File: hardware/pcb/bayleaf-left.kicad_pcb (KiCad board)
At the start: 2 copper layers, 135.5 x 89.5 mm, 64 parts, among them SW1 PG1316S, SW10 PG1316S, SW11 PG1316S, SW12 PG1316S, SW13 PG1316S, SW14 PG1316S, SW15 PG1316S, SW16 PG1316S, SW17 PG1316S, SW18 PG1316S, SW19 PG1316S, SW2 PG1316S, SW20 PG1316S, SW21 PG1316S, SW22 PG1316S, SW23 PG1316S, SW24 PG1316S, SW25 PG1316S, SW26 PG1316S, SW27 PG1316S, SW28 PG1316S, SW29 PG1316S, SW3 PG1316S, SW30 PG1316S, SW31 TS-1187A-B-A-B, SW32 MSK12C02, SW4 PG1316S, SW5 PG1316S, SW6 PG1316S, SW7 PG1316S, SW8 PG1316S, SW9 PG1316S, U1 nice!nano v2

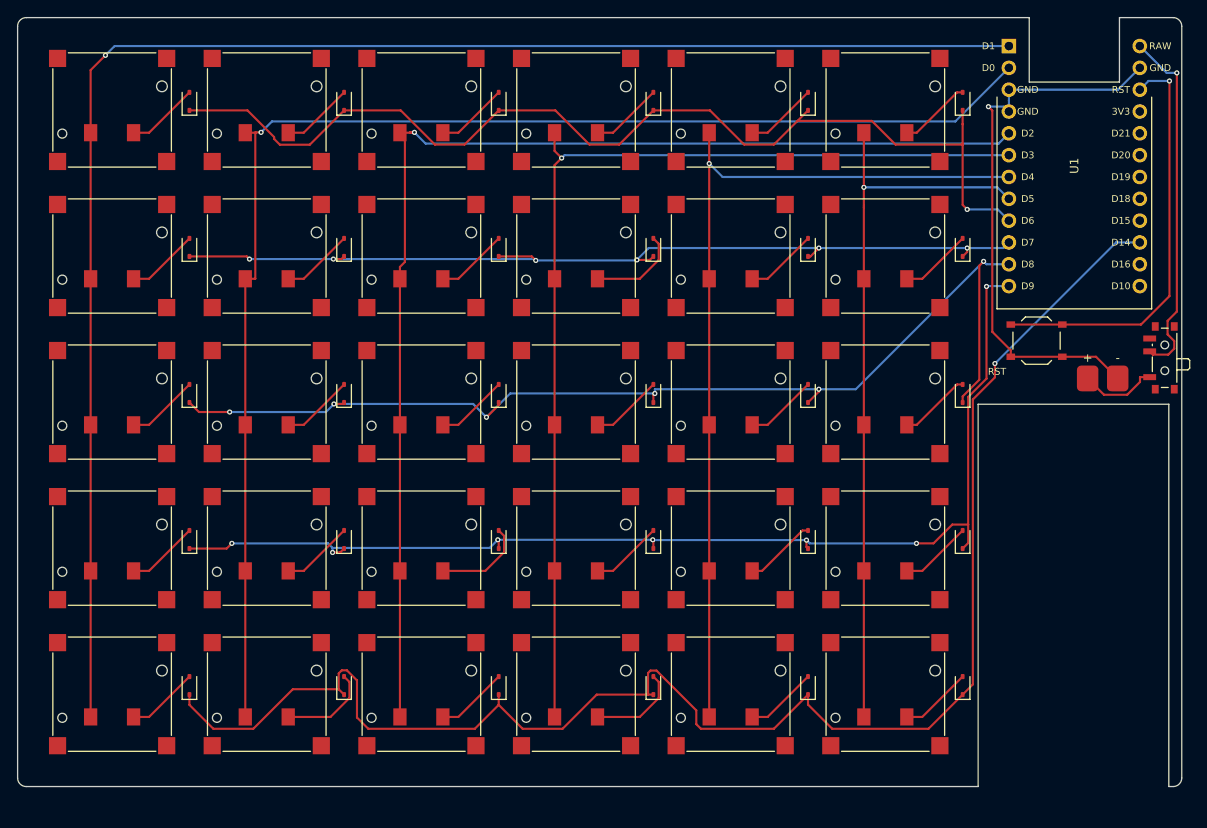
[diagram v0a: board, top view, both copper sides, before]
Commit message: Case: rebuild after the original's MK5 drawing (shell + lid over controller)
- hardware/case: top shell with 103 x 86 key window, 2 mm divider, 27 mm
  controller bay closed by a 0.8 mm roof, 6.2 -> 3.8 mm front curve, drafted
  walls, 7 tapped M2 bosses; separate 0.8 mm bottom plate screwed into them
- PCB: 17 mm pitch to fit the window, SOD-523 diodes, nice!nano rotated so
  USB-C exits the front, 402040 cell under the roof, 2.2 mm holes + copper
  keep-outs at the bosses, per-half matrix pin map; both halves route clean
- firmware: per-half kscan pins in the left/right overlays
- docs: case-drawing notes, BOM/ordering/assembly/schematic, new renders

Co-Authored-By: Claude Opus 5.5 <noreply@anthropic.com>
Claude-Session: https://claude.ai/code/session_01C1HRLCKaYQawWFomwAvAgT
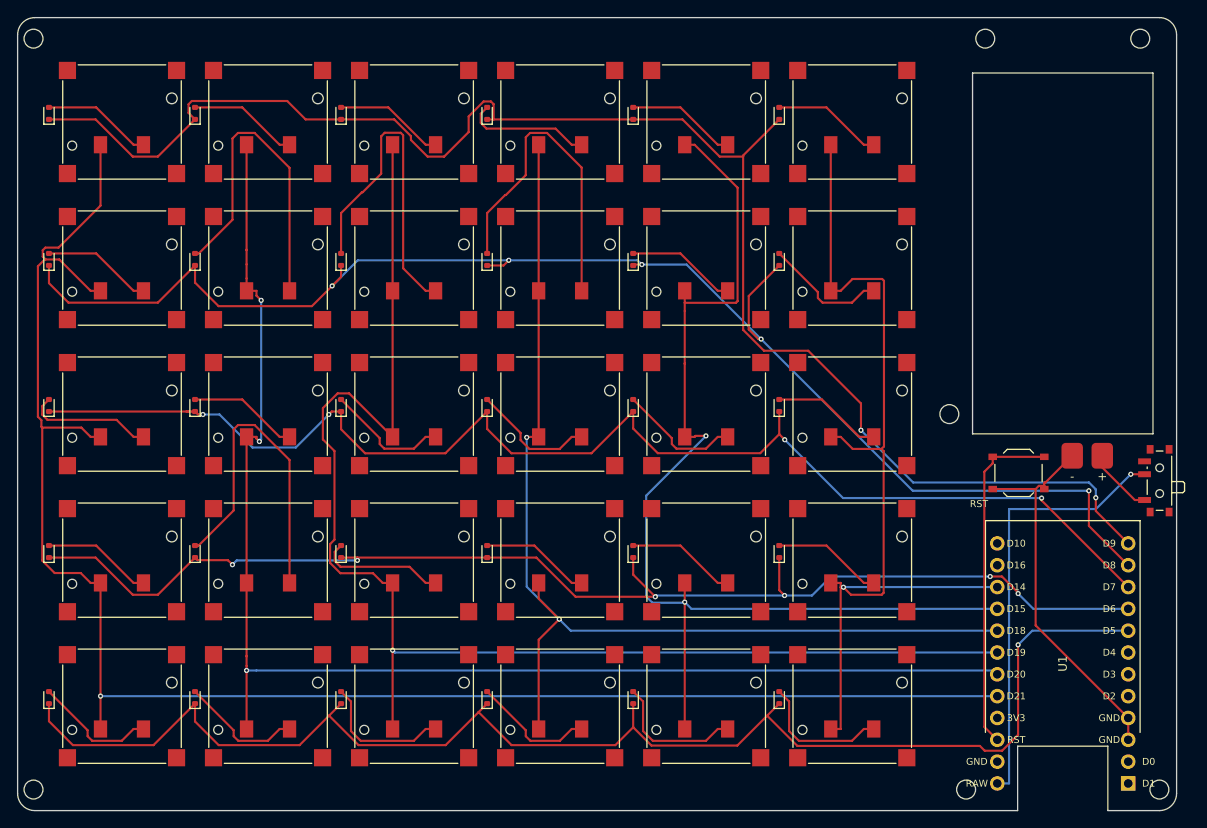
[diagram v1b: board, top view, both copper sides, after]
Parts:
- added H1: boss 6, MountingHole:MountingHole_2.2mm_M2, F.Cu at (1.85, 2.45)
- added H2: boss 6, MountingHole:MountingHole_2.2mm_M2, F.Cu at (1.85, 89.8)
- added H3: boss 6, MountingHole:MountingHole_2.2mm_M2, F.Cu at (112.6, 2.45)
- added H4: boss 6, MountingHole:MountingHole_2.2mm_M2, F.Cu at (130.7, 2.45)
- added H5: boss 6, MountingHole:MountingHole_2.2mm_M2, F.Cu at (108.5, 46.1)
- added H6: boss 4, MountingHole:MountingHole_2.2mm_M2, F.Cu at (110.4, 89.8)
- added H7: boss 4, MountingHole:MountingHole_2.2mm_M2, F.Cu at (132.9, 89.8)
- D1, D10, D11, D12, D13, D14, D15, D16, D17, D18, D19, D2, D20, D21, D22, D23, D24, D25, D26, D27, D28, D29, D3, D30, D4, D5, D6, D7, D8, D9: value 1N4148WS -> 1N4148WT; footprint Diode_SMD:D_SOD-323 -> Diode_SMD:D_SOD-523
- moved U1 58.0 mm to (121.7, 75.2), turned to 180 degrees
- moved D12 21.4 mm to (88.7, 28.1)
- moved D18 21.4 mm to (88.7, 45.1)
- moved D24 21.4 mm to (88.7, 62.1)
- moved D30 21.4 mm to (88.7, 79.2)
- moved D6 21.4 mm to (88.7, 11.2)
- moved D11 20.4 mm to (71.7, 28.1)
- moved D17 20.4 mm to (71.7, 45.1)
- moved D23 20.4 mm to (71.7, 62.1)
- moved D29 20.4 mm to (71.7, 79.2)
- moved D5 20.4 mm to (71.7, 11.2)
- moved D10 19.4 mm to (54.6, 28.1)
- moved D16 19.4 mm to (54.6, 45.1)
- moved D22 19.4 mm to (54.6, 62.1)
- moved D28 19.4 mm to (54.6, 79.2)
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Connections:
- U1 pad 1: COL0 -> (no net)
- U1 pad 10: ROW1 -> ROW2
- U1 pad 11: ROW2 -> ROW1
- U1 pad 12: ROW3 -> ROW0
- U1 pad 14: GND -> (no net)
- U1 pad 17: (no net) -> COL0
- U1 pad 18: (no net) -> COL1
- U1 pad 19: (no net) -> COL2
- U1 pad 2: COL1 -> (no net)
- U1 pad 20: (no net) -> COL3
- U1 pad 21: (no net) -> COL4
- U1 pad 22: ROW4 -> COL5
- U1 pad 5: COL2 -> (no net)
- U1 pad 6: COL3 -> (no net)
- U1 pad 7: COL4 -> (no net)
- U1 pad 8: COL5 -> ROW4
- U1 pad 9: ROW0 -> ROW3
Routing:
- net ROW1: track 107.3 -> 170.3 mm, vias 6 -> 5
- net ROW0: track 122.8 -> 183.1 mm, vias 1 -> 2
- net N_SW9: track 8.45 -> 38.8 mm
- net N_SW8: track 8.45 -> 38.4 mm
- net N_SW20: track 8.45 -> 38.3 mm
- net N_SW10: track 10.8 -> 38.2 mm
- net ROW2: track 129.0 -> 153.8 mm, vias 6 -> 4
- net COL5: track 85.4 -> 109.6 mm
- net COL4: track 103.5 -> 127.3 mm, vias 1 -> 2
- net GND: track 65.1 -> 45.1 mm, vias 1 -> 0
- net COL2: track 140.8 -> 159.4 mm
- net ROW4: track 183.0 -> 165.0 mm
- net ROW3: track 132.2 -> 146.8 mm, vias 7 -> 6
- net COL0: track 183.3 -> 197.2 mm
- net RAW: track 41.8 -> 50.8 mm
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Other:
- board size 135.5 x 89.5 mm -> 134.9 x 92.3 mm
- board text added: "LiPo 4.0x20x40"
- board text removed: "LiPo 3.0x20x40"

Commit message: Case: match the build photos - 5 mm tall, separate controller lid
- shell: 3.8 mm frame around the key window curving up to 4.1 mm at the
  controller end; controller bay now open on top; all posts M2 x 2
- new lid part: 0.8 mm plate over the bay, flush with the outer edges, taped
  on; its top is the 5.0 mm tallest point (contrast anodised like the original)
- 302040 cell (bay under the lid is 3.4 mm), 14 x M2x3 screws
- renders: silver shell, blue lid, blank caps; desk/front views like the photos
- docs/BOM/README updated; PCB unchanged

Co-Authored-By: Claude Opus 5.5 <noreply@anthropic.com>
Claude-Session: https://claude.ai/code/session_01C1HRLCKaYQawWFomwAvAgT
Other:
- board text added: "LiPo 3.0x20x40"
- board text removed: "LiPo 4.0x20x40"
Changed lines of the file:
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@@
     (effects (font (size 0.8 0.8) (thickness 0.12)))
   )
-  (gr_text "LiPo 4.0x20x40" (at 121.65 27) (layer "Cmts.User")
+  (gr_text "LiPo 3.0x20x40" (at 121.65 27) (layer "Cmts.User")
     (effects (font (size 0.9 0.9) (thickness 0.135)))
   )

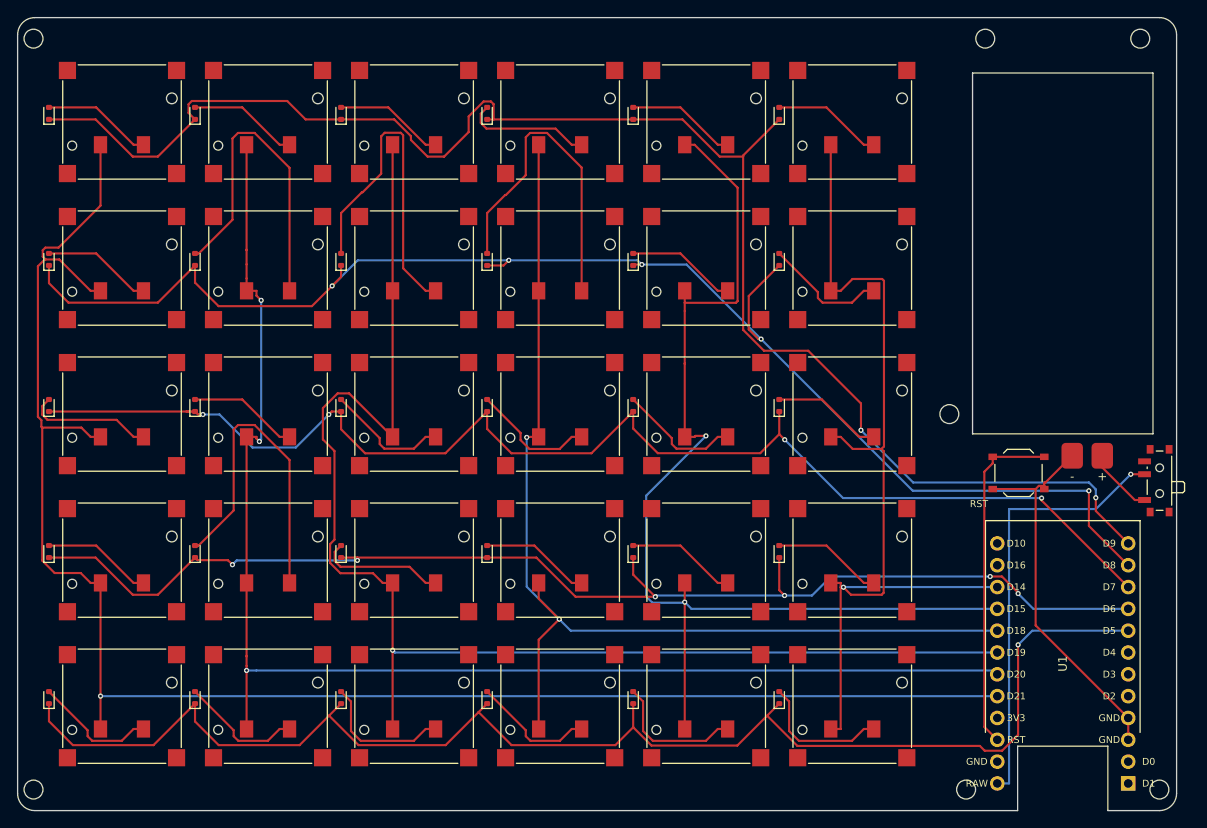
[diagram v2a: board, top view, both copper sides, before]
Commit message: Case: one-piece shell from the sketchpad shape (3.2 mm rim, 5.0 mm plateau, S-bends)
- case.py: top surface = blurred square plateau (x >= 96.5, y <= 76) over a 3.2 mm rim;
  controller roofed by the shell (no lid), R2 key-window corners, USB-C in the back wall,
  reset pin-hole, per-post thread depths (2 mm / 1.1 mm)
- PCB: nice!nano USB-C facing the back, KMR2 reset and slide switch beside it, 302030 cell
  window in front of it; rerouted, fab outputs regenerated
- firmware: per-half matrix pins to match the new layout
- docs: sketchpad shape saved, renders, BOM/ordering/assembly/case/schematic updated

Co-Authored-By: Claude Opus 5.5 <noreply@anthropic.com>
Claude-Session: https://claude.ai/code/session_01C1HRLCKaYQawWFomwAvAgT
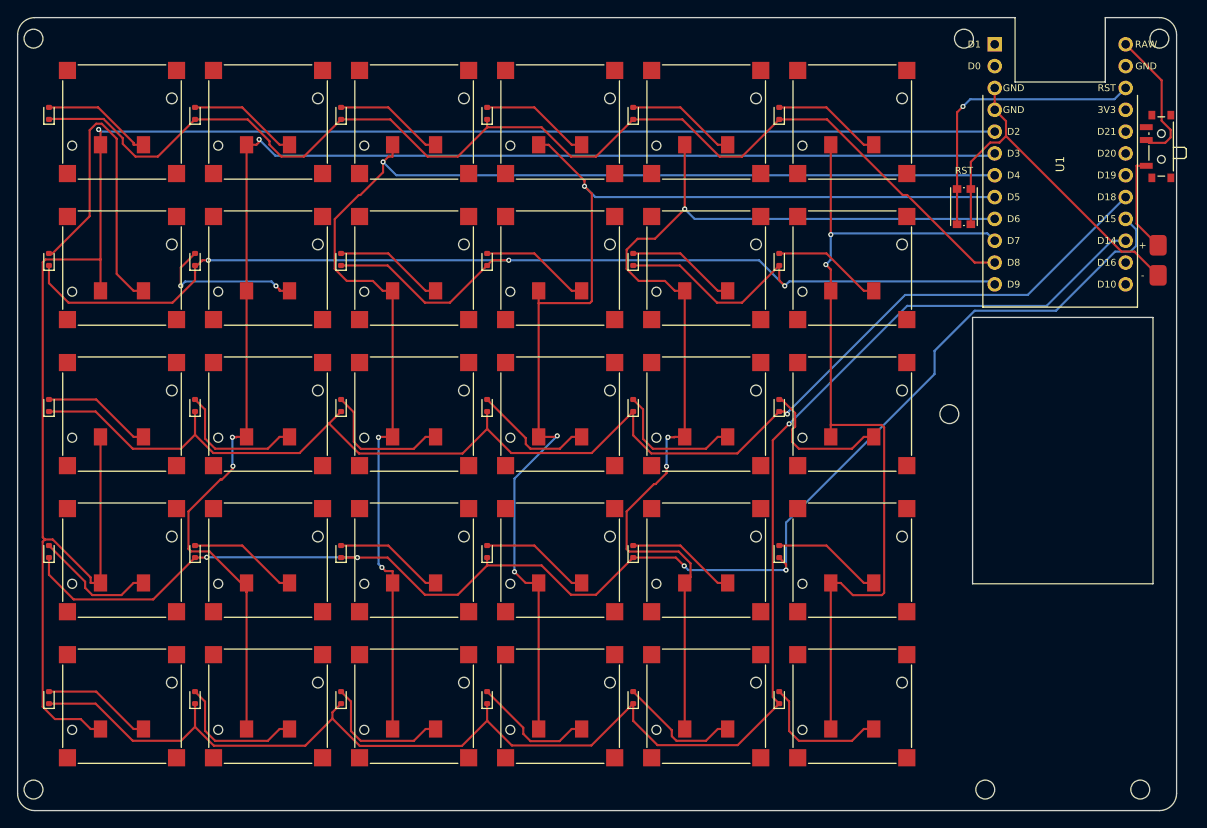
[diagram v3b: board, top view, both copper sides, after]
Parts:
- BT1: footprint bayleaf:Battery_Pads -> bayleaf:Battery_Pads_Small
- H3, H4: value boss 6 -> boss 4
- H6, H7: value boss 4 -> boss 6
- SW31: value TS-1187A-B-A-B -> KMR211NGLFS; footprint Button_Switch_SMD:SW_Push_1P1T_XKB_TS-1187A -> Button_Switch_SMD:SW_Push_1P1T_NO_CK_KMR2
- moved U1 58.2 mm to (121.3, 17.0), turned to 0 degrees
- moved SW32 38.9 mm to (132.8, 15.0)
- moved SW31 31.6 mm to (110.2, 22.0), turned to 90 degrees
- moved BT1 24.2 mm to (132.8, 28.2), turned to 0 degrees
- moved H3 2.48 mm to (110.2, 2.45)
- moved H4 2.23 mm to (132.9, 2.45)
- moved H7 2.23 mm to (130.7, 89.8)
- moved H6 2.23 mm to (112.6, 89.8)
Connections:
- U1 pad 10: ROW2 -> COL5
- U1 pad 11: ROW1 -> ROW0
- U1 pad 12: ROW0 -> ROW1
- U1 pad 17: COL0 -> (no net)
- U1 pad 18: COL1 -> (no net)
- U1 pad 19: COL2 -> (no net)
- U1 pad 20: COL3 -> ROW2
- U1 pad 21: COL4 -> ROW3
- U1 pad 22: COL5 -> ROW4
- U1 pad 5: (no net) -> COL0
- U1 pad 6: (no net) -> COL1
- U1 pad 7: (no net) -> COL2
- U1 pad 8: ROW4 -> COL3
- U1 pad 9: ROW3 -> COL4
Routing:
- net ROW0: track 183.1 -> 135.7 mm, vias 2 -> 0
- net RAW: track 50.8 -> 16.2 mm, vias 1 -> 0
- net N_SW7: track 12.8 -> 40.4 mm
- net N_SW9: track 38.8 -> 12.8 mm
- net N_SW20: track 38.3 -> 12.8 mm
- net N_SW10: track 38.2 -> 12.8 mm
- net ROW4: track 165.0 -> 189.1 mm
- net ROW3: track 146.8 -> 167.5 mm, vias 6 -> 4
- net N_SW8: track 38.4 -> 17.9 mm, vias 0 -> 2
- net COL0: track 197.2 -> 215.8 mm
- net COL2: track 159.4 -> 151.0 mm, vias 1 -> 3
- net RST: track 40.0 -> 33.8 mm, vias 0 -> 1
- net COL5: track 109.6 -> 103.5 mm, vias 1 -> 2
- net COL1: track 159.8 -> 165.4 mm
- net ROW1: track 170.3 -> 165.0 mm, vias 5 -> 3
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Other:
- outline, holes or cut-outs redrawn
- board text added: "LiPo 3.0x20x30"
- board text removed: "LiPo 3.0x20x40"

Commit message: Drop the power switch, stadium USB-C opening, straight-wall + chamfer case variant
- PCB: no slide switch; the cell feeds the nice!nano RAW pin directly (ZMK deep sleep);
  rerouted, 0 unconnected, courtyard warning gone
- case: obround USB-C opening concentric with the receptacle (continues into the plate
  edge), no switch slot; new bayleaf-shell-*-chamfer variant with vertical walls and a
  1 mm 45 deg chamfer on the top edge that follows the blended surface
- renders: obround receptacle, compare.jpg (drafted vs chamfer); docs and BOM updated

Co-Authored-By: Claude Opus 5.5 <noreply@anthropic.com>
Claude-Session: https://claude.ai/code/session_01C1HRLCKaYQawWFomwAvAgT
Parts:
- removed SW32: MSK12C02, Button_Switch_SMD:SW_SPDT_PCM12
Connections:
- BT1 pad 1: BAT+ -> RAW
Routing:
- net COL1: track 165.4 -> 194.2 mm, vias 3 -> 1
- net ROW2: track 158.9 -> 186.4 mm, vias 1 -> 3
- net N_SW7: track 40.4 -> 14.4 mm
- net ROW3: track 167.5 -> 190.6 mm
- net COL2: track 151.0 -> 172.9 mm, vias 3 -> 1
- net COL0: track 215.8 -> 197.6 mm
- net BAT+: track 11.4 -> 0.00 mm
- net RAW: track 16.2 -> 25.0 mm
- net ROW1: track 165.0 -> 157.8 mm
- net N_SW8: track 17.9 -> 12.8 mm, vias 2 -> 0
- net N_SW24: track 12.8 -> 17.6 mm, vias 0 -> 2
- net COL3: track 133.4 -> 129.2 mm, vias 3 -> 1
- net N_SW2: track 12.8 -> 16.6 mm
- net COL4: track 124.6 -> 120.9 mm, vias 3 -> 2
- net N_SW18: track 16.4 -> 12.8 mm
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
